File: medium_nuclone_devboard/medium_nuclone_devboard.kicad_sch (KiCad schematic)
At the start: 39 parts, among them J1 JTAG_2X05, J2 TYPE-C-31-M-12, J3 nuclone_medium_left, J4 nuclone_medium_right, SW1 RESET, SW2 Bootloader, U1 MCP1702-MB

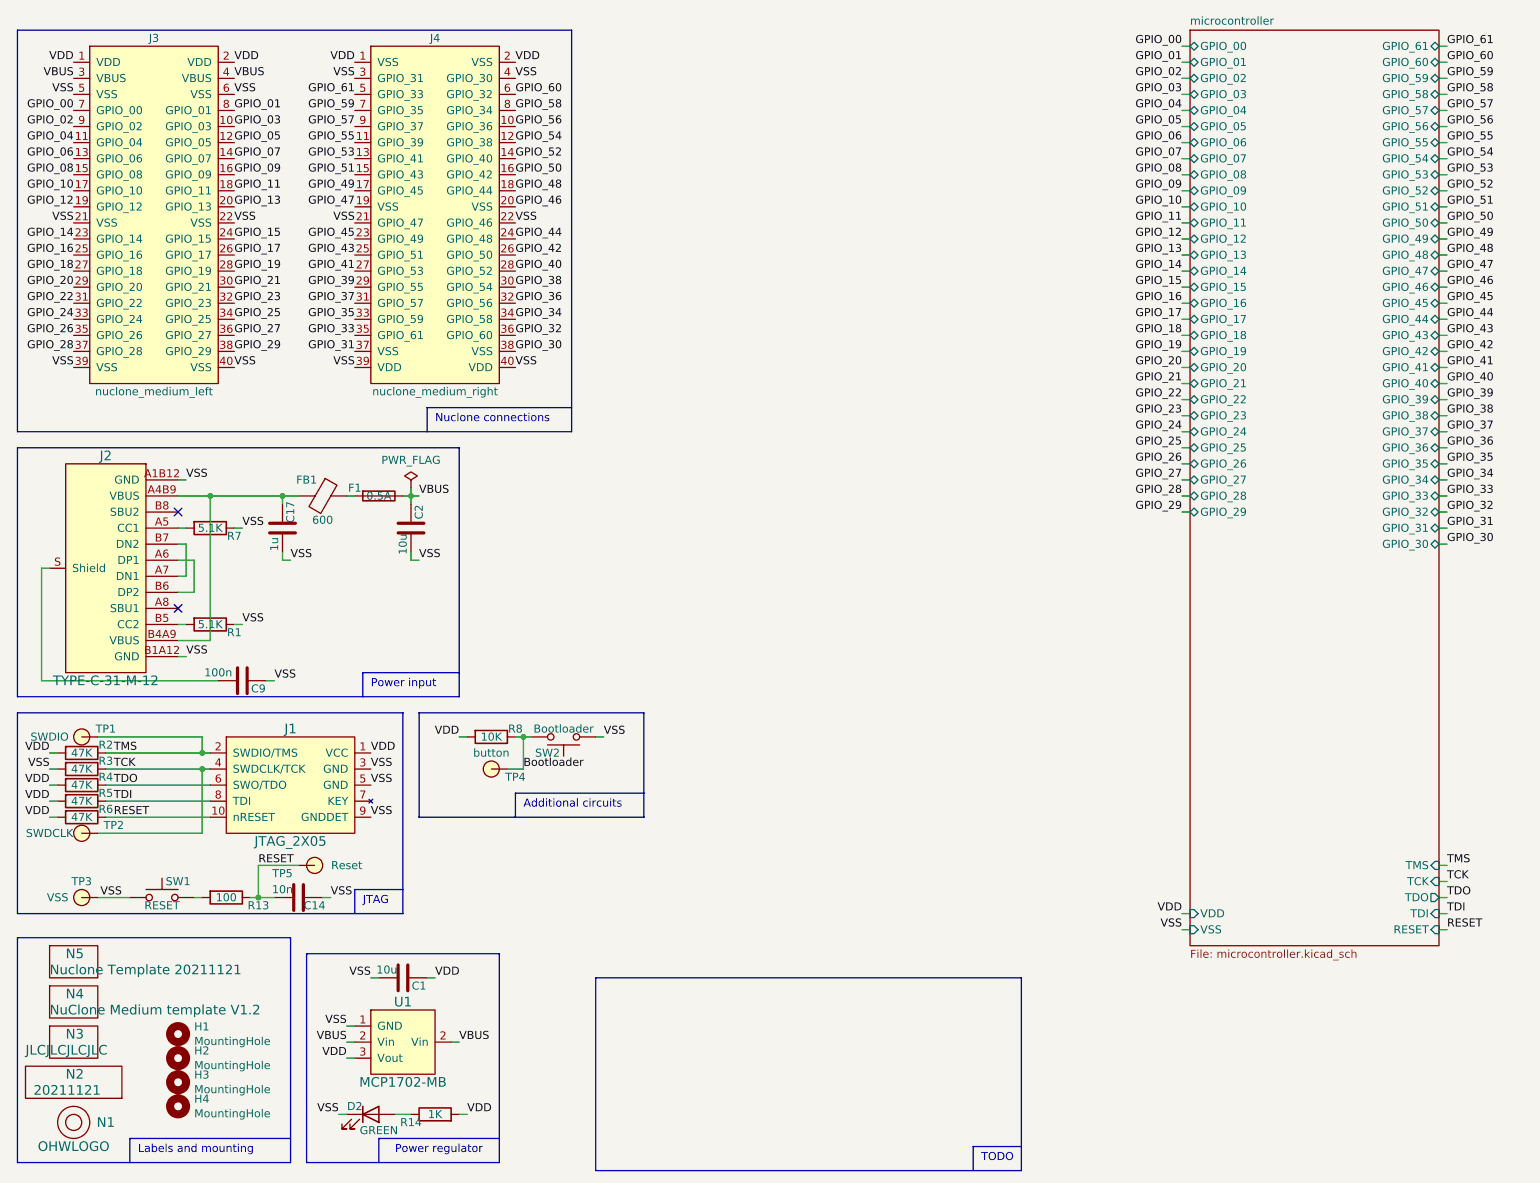
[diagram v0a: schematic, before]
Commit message: imported aisler simple design rules
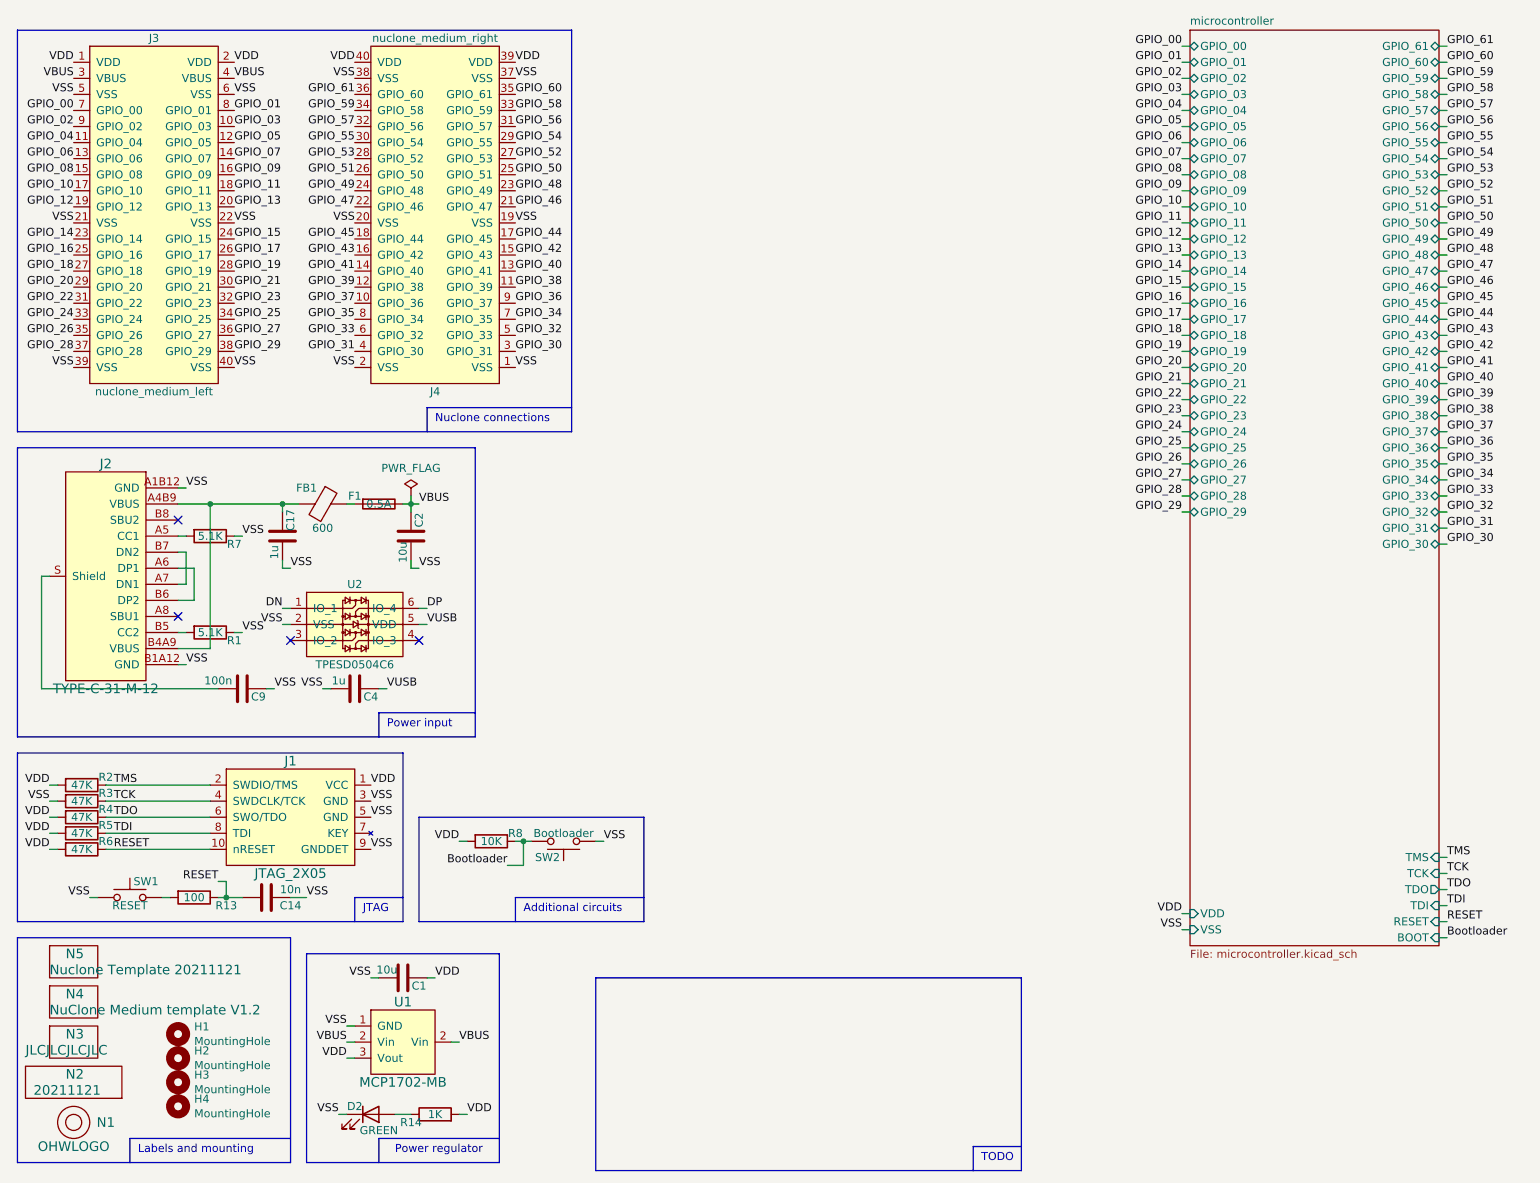
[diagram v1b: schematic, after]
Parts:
- removed TP1: SWDIO, SquantorTestPoints:TestPoint_hole_H04R07, symbol SquantorProto:testpad
- removed TP2: SWDCLK, SquantorTestPoints:TestPoint_hole_H04R07, symbol SquantorProto:testpad
- removed TP3: VSS, SquantorTestPoints:TestPoint_hole_H05R10, symbol SquantorProto:testpad
- removed TP4: button, SquantorTestPoints:TestPoint_hole_H04R07, symbol SquantorProto:testpad
- removed TP5: Reset, SquantorTestPoints:TestPoint_hole_H04R07, symbol SquantorProto:testpad
- added C4: 1u, SquantorRcl:C_0402, symbol Device:C
- added U2: TPESD0504C6, SquantorIC:SOT363-ONsemi, symbol SquantorDevice:TVS_4_Array
- H1, H2, H3, H4: footprint MountingHole:MountingHole_3.2mm_M3_Pad_Via -> SquantorPcbOutline:MountingHole_3.2mm_M3_Pad_Via
- N1: footprint Symbols:OSHW-Symbol_6.7x6mm_SilkScreen -> Symbol:OSHW-Symbol_6.7x6mm_SilkScreen
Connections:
- net GPIO_30: now also J4.3 (GPIO_31); no longer J4.38 (VSS)
- net GPIO_31: now also J4.4 (GPIO_30); no longer J4.37 (VSS)
- net GPIO_32: now also J4.5 (GPIO_33); no longer J4.36 (GPIO_60)
- net GPIO_33: now also J4.6 (GPIO_32); no longer J4.35 (GPIO_61)
- net GPIO_34: now also J4.7 (GPIO_35); no longer J4.34 (GPIO_58)
- net GPIO_35: now also J4.8 (GPIO_34); no longer J4.33 (GPIO_59)
- net GPIO_36: now also J4.9 (GPIO_37); no longer J4.32 (GPIO_56)
- net GPIO_37: now also J4.10 (GPIO_36); no longer J4.31 (GPIO_57)
- net GPIO_38: now also J4.11 (GPIO_39); no longer J4.30 (GPIO_54)
- net GPIO_39: now also J4.12 (GPIO_38); no longer J4.29 (GPIO_55)
- net GPIO_40: now also J4.13 (GPIO_41); no longer J4.28 (GPIO_52)
- net GPIO_41: now also J4.14 (GPIO_40); no longer J4.27 (GPIO_53)
- net GPIO_42: now also J4.15 (GPIO_43); no longer J4.26 (GPIO_50)
- net GPIO_43: now also J4.16 (GPIO_42); no longer J4.25 (GPIO_51)
- net GPIO_44: now also J4.17 (GPIO_45); no longer J4.24 (GPIO_48)
- net GPIO_45: now also J4.18 (GPIO_44); no longer J4.23 (GPIO_49)
- net GPIO_46: now also J4.21 (GPIO_47); no longer J4.20 (VSS)
- net GPIO_47: now also J4.22 (GPIO_46); no longer J4.19 (VSS)
- net GPIO_48: now also J4.23 (GPIO_49); no longer J4.18 (GPIO_44)
- net GPIO_49: now also J4.24 (GPIO_48); no longer J4.17 (GPIO_45)
- net GPIO_50: now also J4.25 (GPIO_51); no longer J4.16 (GPIO_42)
- net GPIO_51: now also J4.26 (GPIO_50); no longer J4.15 (GPIO_43)
- net GPIO_52: now also J4.27 (GPIO_53); no longer J4.14 (GPIO_40)
- net GPIO_53: now also J4.28 (GPIO_52); no longer J4.13 (GPIO_41)
- net GPIO_54: now also J4.29 (GPIO_55); no longer J4.12 (GPIO_38)
- net GPIO_55: now also J4.30 (GPIO_54); no longer J4.11 (GPIO_39)
- net GPIO_56: now also J4.31 (GPIO_57); no longer J4.10 (GPIO_36)
- net GPIO_57: now also J4.32 (GPIO_56); no longer J4.9 (GPIO_37)
- net GPIO_58: now also J4.33 (GPIO_59); no longer J4.8 (GPIO_34)
- net GPIO_59: now also J4.34 (GPIO_58); no longer J4.7 (GPIO_35)
- net GPIO_60: now also J4.35 (GPIO_61); no longer J4.6 (GPIO_32)
- net GPIO_61: now also J4.36 (GPIO_60); no longer J4.5 (GPIO_33)
- net VDD: now also J4.39 (VDD), J4.40 (VDD); no longer J4.1 (VSS), J4.2 (VSS)
- net VSS: now also J4.1 (VSS), J4.19 (VSS), J4.2 (VSS), J4.20 (VSS), J4.37 (VSS), J4.38 (VSS), C4.2, U2.2 (VSS); no longer J4.21 (GPIO_47), J4.22 (GPIO_46), J4.3 (GPIO_31), J4.39 (VDD), J4.4 (GPIO_30), J4.40 (VDD)
- new net DN: U2.1 (IO_1)
- new net DP: U2.6 (IO_4)
- new net VUSB: C4.1, U2.5 (VDD)
- no-connect marks 2 -> 4
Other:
- sheet microcontroller ports: added BOOT; removed none
- moved on the sheet: C14, C17, C2, C9, F1, FB1, J1, J2, J4, R1, R13, R2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
